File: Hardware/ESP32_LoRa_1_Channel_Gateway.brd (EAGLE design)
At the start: 25.4 x 45.7 mm, 86 parts, among them J1 USB, J2 U.FL, J6 QWIIC, Q1 MBT3904DW1T1, U1 3.3V, U2 ESP-WROOM-32NARROW, U3 CH340C, U4 RFM95W

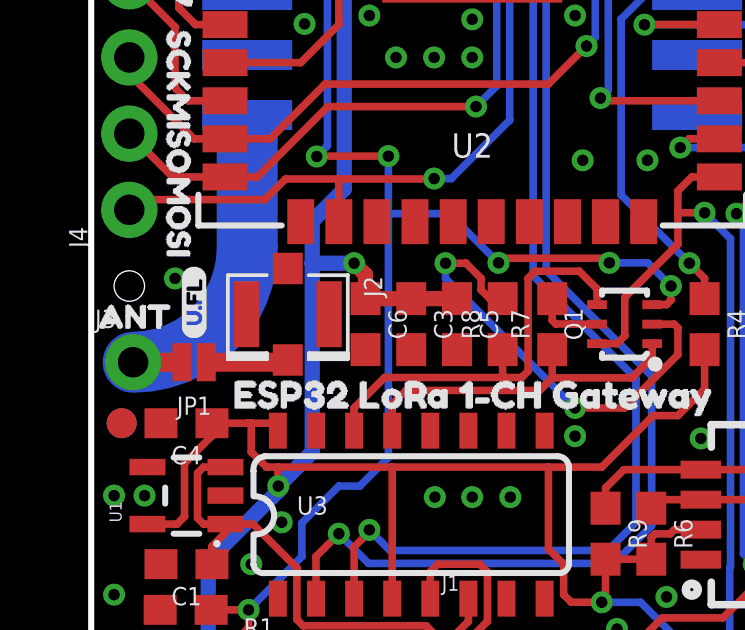
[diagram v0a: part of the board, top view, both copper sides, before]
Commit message: Fixed U.FL location (cleared away form 0603 package)
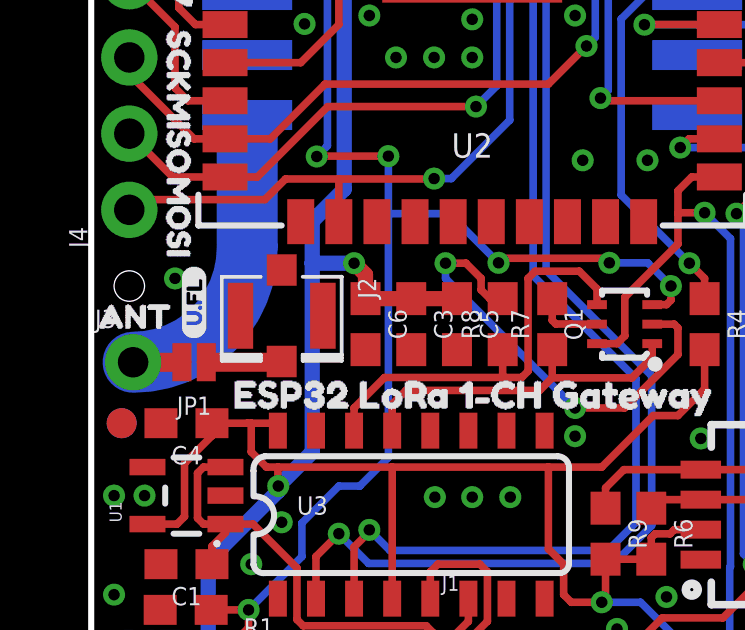
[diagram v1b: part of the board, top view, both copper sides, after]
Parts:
- moved J2 0.21 mm to (6.35, 16.8)
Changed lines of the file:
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@@
 <setting verticaltext="up"/>
 </settings>
-<grid distance="0.05" unitdist="inch" unit="inch" style="lines" multiple="1" display="yes" altdistance="0.005" altunitdist="inch" altunit="inch"/>
+<grid distance="0.05" unitdist="inch" unit="inch" style="lines" multiple="1" display="yes" altdistance="0.001" altunitdist="inch" altunit="inch"/>
 <layers>
-<layer number="1" name="Top" color="4" fill="1" visible="no" active="yes"/>
-<layer number="16" name="Bottom" color="1" fill="1" visible="no" active="yes"/>
+<layer number="1" name="Top" color="4" fill="1" visible="yes" active="yes"/>
+<layer number="16" name="Bottom" color="1" fill="1" visible="yes" active="yes"/>
 <layer number="17" name="Pads" color="2" fill="1" visible="yes" active="yes"/>
-<layer number="18" name="Vias" color="2" fill="1" visible="no" active="yes"/>
-<layer number="19" name="Unrouted" color="6" fill="1" visible="no" active="yes"/>
+<layer number="18" name="Vias" color="2" fill="1" visible="yes" active="yes"/>
+<layer number="19" name="Unrouted" color="6" fill="1" visible="yes" active="yes"/>
 <layer number="20" name="Dimension" color="15" fill="1" visible="yes" active="yes"/>
-<layer number="21" name="tPlace" color="16" fill="1" visible="no" active="yes"/>
-<layer number="22" name="bPlace" color="14" fill="1" visible="no" active="yes"/>
+<layer number="21" name="tPlace" color="16" fill="1" visible="yes" active="yes"/>
+<layer number="22" name="bPlace" color="14" fill="1" visible="yes" active="yes"/>
 <layer number="23" name="tOrigins" color="15" fill="1" visible="yes" active="yes"/>
-<layer number="24" name="bOrigins" color="15" fill="1" visible="no" active="yes"/>
-<layer number="25" name="tNames" color="7" fill="1" visible="no" active="yes"/>
-<layer number="26" name="bNames" color="7" fill="1" visible="no" active="yes"/>
+<layer number="24" name="bOrigins" color="15" fill="1" visible="yes" active="yes"/>
+<layer number="25" name="tNames" color="7" fill="1" visible="yes" active="yes"/>
+<layer number="26" name="bNames" color="7" fill="1" visible="yes" active="yes"/>
 <layer number="27" name="tValues" color="7" fill="1" visible="yes" active="yes"/>
-<layer number="28" name="bValues" color="7" fill="1" visible="no" active="yes"/>
-<layer number="29" name="tStop" color="7" fill="3" visible="no" active="yes"/>
-<layer number="30" name="bStop" color="7" fill="6" visible="no" active="yes"/>
+<layer number="28" name="bValues" color="7" fill="1" visible="yes" active="yes"/>
+<layer number="29" name="tStop" color="7" fill="3" visible="yes" active="yes"/>
+<layer number="30" name="bStop" color="7" fill="6" visible="yes" active="yes"/>
 <layer number="31" name="tCream" color="7" fill="4" visible="yes" active="yes"/>
-<layer number="32" name="bCream" color="7" fill="5" visible="no" active="yes"/>
-<layer number="33" name="tFinish" color="6" fill="3" visible="no" active="yes"/>
-<layer number="34" name="bFinish" color="6" fill="6" visible="no" active="yes"/>
-<layer number="35" name="tGlue" color="7" fill="4" visible="no" active="yes"/>
-<layer number="36" name="bGlue" color="7" fill="5" visible="no" active="yes"/>
-<layer number="37" name="tTest" color="7" fill="1" visible="no" active="yes"/>
-<layer number="38" name="bTest" color="7" fill="1" visible="no" active="yes"/>
-<layer number="39" name="tKeepout" color="4" fill="11" visible="no" active="yes"/>
-<layer number="40" name="bKeepout" color="1" fill="11" visible="no" active="yes"/>
-<layer number="41" name="tRestrict" color="4" fill="10" visible="no" active="yes"/>
-<layer number="42" name="bRestrict" color="1" fill="10" visible="no" active="yes"/>
-<layer number="43" name="vRestrict" color="2" fill="10" visible="no" active="yes"/>
-<layer number="44" name="Drills" color="7" fill="1" visible="no" active="yes"/>
+<layer number="32" name="bCream" color="7" fill="5" visible="yes" active="yes"/>
+<layer number="33" name="tFinish" color="6" fill="3" visible="yes" active="yes"/>
+<layer number="34" name="bFinish" color="6" fill="6" visible="yes" active="yes"/>
+<layer number="35" name="tGlue" color="7" fill="4" visible="yes" active="yes"/>
+<layer number="36" name="bGlue" color="7" fill="5" visible="yes" active="yes"/>
+<layer number="37" name="tTest" color="7" fill="1" visible="yes" active="yes"/>
+<layer number="38" name="bTest" color="7" fill="1" visible="yes" active="yes"/>
+<layer number="39" name="tKeepout" color="4" fill="11" visible="yes" active="yes"/>
+<layer number="40" name="bKeepout" color="1" fill="11" visible="yes" active="yes"/>
+<layer number="41" name="tRestrict" color="4" fill="10" visible="yes" active="yes"/>
+<layer number="42" name="bRestrict" color="1" fill="10" visible="yes" active="yes"/>
+<layer number="43" name="vRestrict" color="2" fill="10" visible="yes" active="yes"/>
+<layer number="44" name="Drills" color="7" fill="1" visible="yes" active="yes"/>
 <layer number="45" name="Holes" color="7" fill="1" visible="yes" active="yes"/>
-<layer number="46" name="Milling" color="3" fill="1" visible="no" active="yes"/>
-<layer number="47" name="Measures" color="7" fill="1" visible="no" active="yes"/>
-<layer number="48" name="Document" color="7" fill="1" visible="no" active="yes"/>
-<layer number="49" name="Reference" color="7" fill="1" visible="no" active="yes"/>
-<layer number="50" name="dxf" color="7" fill="1" visible="no" active="yes"/>
+<layer number="46" name="Milling" color="3" fill="1" visible="yes" active="yes"/>
+<layer number="47" name="Measures" color="7" fill="1" visible="yes" active="yes"/>
+<layer number="48" name="Document" color="7" fill="1" visible="yes" active="yes"/>
+<layer number="49" name="Reference" color="7" fill="1" visible="yes" active="yes"/>
+<layer number="50" name="dxf" color="7" fill="1" visible="yes" active="yes"/>
 <layer number="51" name="tDocu" color="6" fill="1" visible="yes" active="yes"/>
-<layer number="52" name="bDocu" color="7" fill="1" visible="no" active="yes"/>
+<layer number="52" name="bDocu" color="7" fill="1" visible="yes" active="yes"/>
 <layer number="91" name="Nets" color="2" fill="1" visible="no" active="no"/>
 <layer number="92" name="Busses" color="1" fill="1" visible="no" active="no"/>
@@
 <layer number="95" name="Names" color="7" fill="1" visible="no" active="no"/>
 <layer number="96" name="Values" color="7" fill="1" visible="no" active="no"/>
-<layer number="2" name="Route2" color="1" fill="3" visible="no" active="yes"/>
-<layer number="15" name="Route15" color="4" fill="6" visible="no" active="yes"/>
+<layer number="2" name="Route2" color="1" fill="3" visible="yes" active="yes"/>
+<layer number="15" name="Route15" color="4" fill="6" visible="yes" active="yes"/>
 <layer number="53" name="tGND_GNDA" color="7" fill="9" visible="no" active="no"/>
 <layer number="54" name="bGND_GNDA" color="1" fill="9" visible="no" active="no"/>
@@
 <attribute name="VALUE" x="17.78" y="4.191" size="0.6096" layer="27" font="vector" ratio="20" rot="R180" align="top-center"/>
 </element>
-<element name="J2" library="SparkFun-Connectors" package="U.FL" value="U.FL" x="6.5532" y="16.8402" smashed="yes" rot="R270">
-<attribute name="NAME" x="9.0932" y="18.1102" size="0.6096" layer="25" font="vector" ratio="20" rot="R270"/>
-<attribute name="PROD_ID" value="CONN-09193" x="42.1132" y="23.1902" size="1.778" layer="27" font="vector" ratio="15" rot="R270" display="off"/>
-<attribute name="SF_ID" value="WRL-09144" x="42.1132" y="23.1902" size="1.778" layer="27" font="vector" ratio="15" rot="R270" display="off"/>
-<attribute name="VALUE" x="5.7658" y="17.0942" size="0.6096" layer="27" font="vector" ratio="20" align="top-left"/>
+<element name="J2" library="SparkFun-Connectors" package="U.FL" value="U.FL" x="6.35" y="16.7894" smashed="yes" rot="R270">
+<attribute name="NAME" x="8.89" y="18.0594" size="0.6096" layer="25" font="vector" ratio="20" rot="R270"/>
+<attribute name="PROD_ID" value="CONN-09193" x="41.91" y="23.1394" size="1.778" layer="27" font="vector" ratio="15" rot="R270" display="off"/>
+<attribute name="SF_ID" value="WRL-09144" x="41.91" y="23.1394" size="1.778" layer="27" font="vector" ratio="15" rot="R270" display="off"/>
+<attribute name="VALUE" x="5.5626" y="17.0434" size="0.6096" layer="27" font="vector" ratio="20" align="top-left"/>
 </element>
 <element name="U3" library="SparkFun-IC-Comms" package="SO016" value="CH340C" x="10.668" y="10.16" smashed="yes">
@@
 <contactref element="JP1" pad="1"/>
 <contactref element="J2" pad="FEED"/>
-<wire x1="3.8354" y1="15.24" x2="6.478" y2="15.24" width="0.635" layer="1"/>
-<wire x1="6.478" y1="15.24" x2="6.5532" y2="15.3152" width="0.635" layer="1" curve="90"/>
+<wire x1="3.8354" y1="15.24" x2="6.3256" y2="15.24" width="0.635" layer="1"/>
+<wire x1="6.3256" y1="15.24" x2="6.35" y2="15.2644" width="0.635" layer="1" curve="90"/>
 </signal>
 </signals>
